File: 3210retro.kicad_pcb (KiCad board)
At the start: 4 copper layers, 44 x 118 mm, 200 parts, among them J1101 MICRO_SD_HINGE, J801 TEST_2P, P101 USB_OTG, P107 HEADPHONE, P109 RUMBLE, P301 SEPS525, P801 JTAG, Q501 MMBF170, Q701 MMBF170, SW701 SW_PUSH, SW702 C, SW703 1, SW704 4ghi, SW705 7pqrs, SW706 -, SW707 2abc, SW708 5jkl, SW709 8tuv, SW710 UP, SW711 3def, SW712 6mno, SW713 9wxyz, SW714 *+, SW715 DOWN, SW716 0space, SW717 #up, U1102 EMIF06-mSD02C3, U1301 LSM9DS1, U201 MAX1555, U202 TPS62742, U203 TPS61021A, U301 TPS61041DBV, U401 LD3985G18R_TSOT23, U402 DRV8601, U403 WM8994ECS/R, U404 MP34DT01TR, U405 MP34DT01TR, U501 SN74AVC2T244, U502 SN74AVC2T244, U503 SN74AVC2T244, U504 A7, U505 SIM_SLOT, U506 SN74AVC2T244, U601 ESP-12E, U801 STM32F756VGTx, X101 ANT_GPS, X102 ANT_GSM, Y801 32kHz, Y802 24MHz

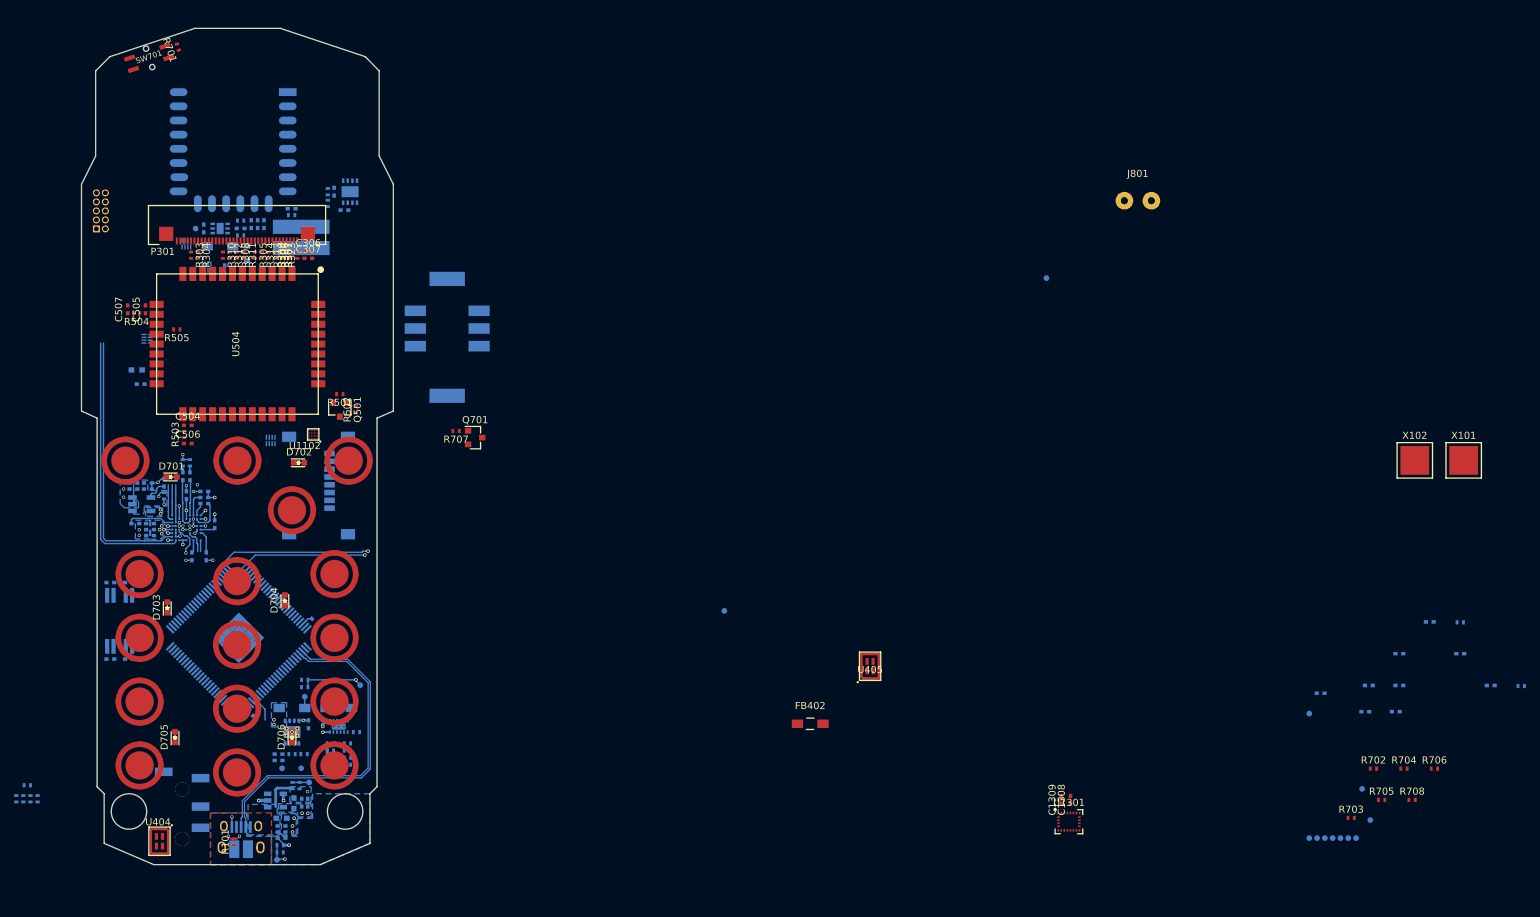
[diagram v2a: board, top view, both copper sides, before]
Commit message: Revision 1 of Layout
6layer board
through-hole via only (0.5/0.3mm drill)
0.2mm track width

https://hackaday.io/project/21263-nokia-3210-retro-fit-board/log/66914-prototype-pcb-done-there-comes-the-review
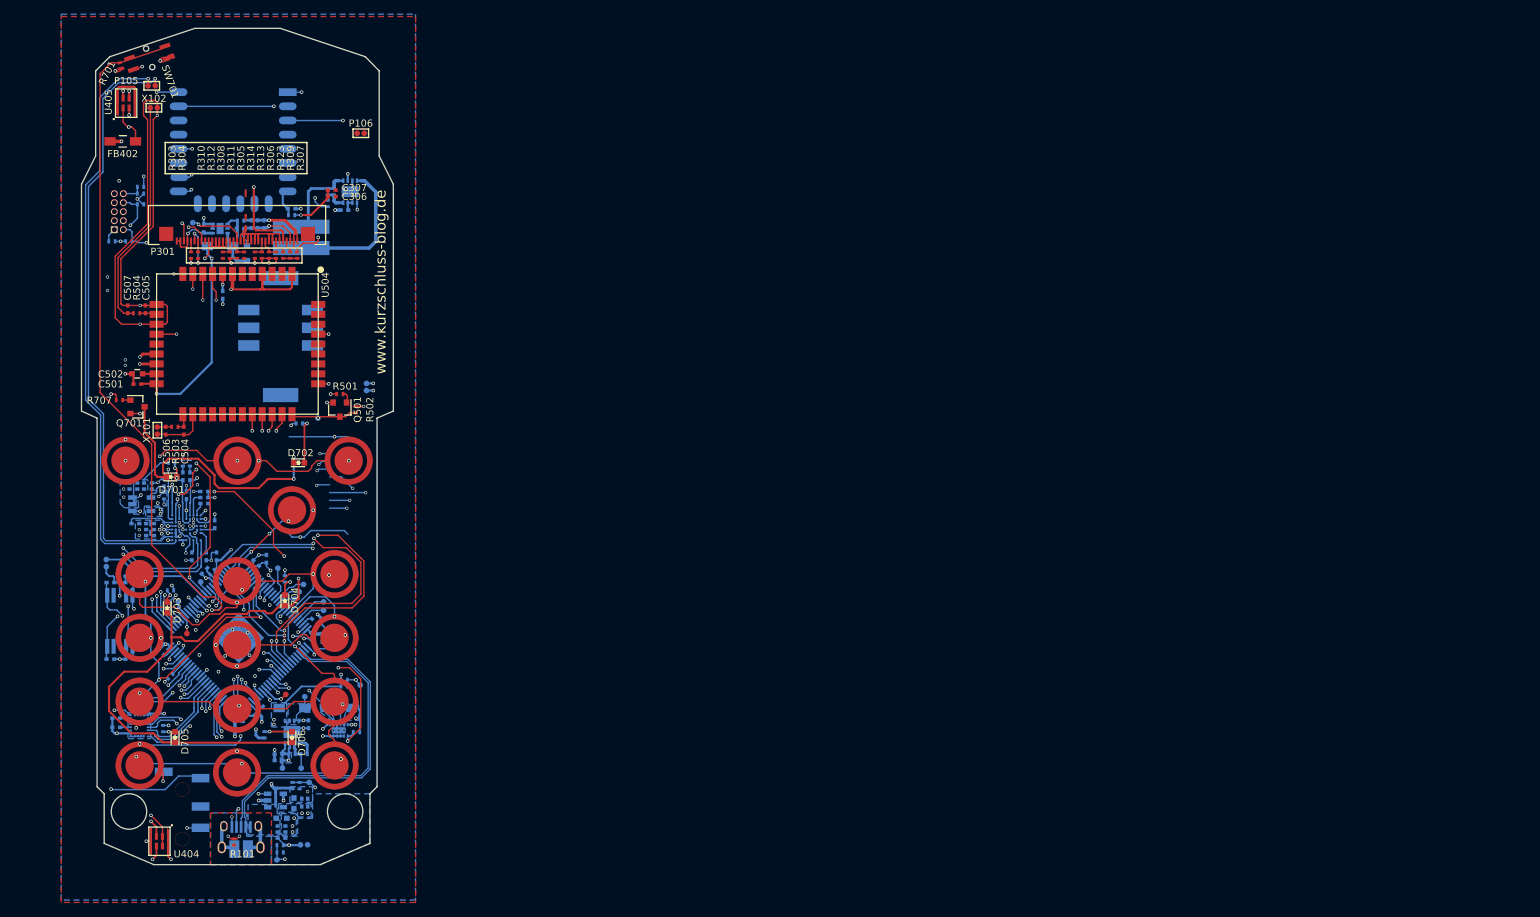
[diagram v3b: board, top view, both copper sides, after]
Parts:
- removed J1101: MICRO_SD_HINGE, Connectors:microSD_Card_Receptacle_Wuerth_693072010801
- removed R205, R206, R209, R210, R211, R212, R213, R214: 0, Resistors_SMD:R_0402_NoSilk
- removed R505: 100, Resistors_SMD:R_0402_NoSilk
- removed TP701, TP702, TP703, TP704, TP705, TP706, TP707, TP708, TP709, TP801: TP, NokiaRetroFit:TP
- removed U1102: EMIF06-mSD02C3, NokiaRetroFit:EMIF06-mSD02C3
- removed U501, U502, U503, U506: SN74AVC2T244, NokiaRetroFit:SN74AVC2T244
- added P103: LIPO, NokiaRetroFit:SolderWirePad_2x_0,8, B.Cu at (117.6, 91.7)
- added P104: DC, NokiaRetroFit:SolderWirePad_2x_0,8, B.Cu at (108.8, 156.3)
- added P105: EAR, NokiaRetroFit:SolderWirePad_2x_0,8, F.Cu at (87.3, 49.2)
- added P106: SPEAKER, NokiaRetroFit:SolderWirePad_2x_0,8, F.Cu at (116.8, 55.9)
- added TP102: TP, NokiaRetroFit:TP, B.Cu at (92.3, 126.5)
- added TP103: TP, NokiaRetroFit:TP, F.Cu at (105.1, 117.3)
- added TP104: TP, NokiaRetroFit:TP, F.Cu at (108.7, 119.6)
- added TP105: TP, NokiaRetroFit:TP, F.Cu at (108.1, 120.6)
- added TP106: TP, NokiaRetroFit:TP, F.Cu at (107.5, 121.6)
- added TP107: TP, NokiaRetroFit:TP, F.Cu at (94.2, 119.2)
- added TP108: TP, NokiaRetroFit:TP, F.Cu at (91.0, 122.0)
- added TP109: TP, NokiaRetroFit:TP, F.Cu at (111.5, 122.0)
- added TP110: TP, NokiaRetroFit:TP, F.Cu at (111.5, 123.2)
- C1308, C1309, R702, R703, R704, R705, R706, R708, TP101, U1301: moved to B.Cu
- C501, C502: moved to F.Cu
- J801: footprint Wire_Pads:SolderWirePad_2x_1mmDrill -> NokiaRetroFit:SolderWirePad_2x_0,8; moved to B.Cu
- U203: footprint Housings_SON:Texas_S-PVSON-N8_ThermalVias -> NokiaRetroFit:Texas_S-PVSON-N8_NoThermalVias
- U404, U405: footprint NokiaRetroFit:MP34DT01 -> NokiaRetroFit:MP34DT01_NoGroundRing
- X101, X102: footprint SMD_Packages:1Pin -> NokiaRetroFit:SolderWirePad_2x_0,8
- moved R803 185.4 mm to (95.8, 117.8), turned to 45 degrees
- moved X102 184.8 mm to (87.6, 52.3)
- moved X101 184.4 mm to (88.1, 97.8), turned to 270 degrees
- moved R802 182.2 mm to (89.9, 132.5), turned to 225 degrees
- moved C805 179.5 mm to (84.1, 118.4), turned to 180 degrees
- moved R706 179.5 mm to (88.9, 139.9), turned to 270 degrees
- moved C814 176.7 mm to (99.6, 138.9)
- moved R704 175.8 mm to (90.0, 120.4), turned to 180 degrees
- moved R702 175.0 mm to (90.1, 102.4)
- moved C815 172.6 mm to (99.6, 138.0)
- moved C809 170.1 mm to (88.6, 129.1), turned to 315 degrees
- moved C808 169.4 mm to (94.7, 117.6), turned to 225 degrees
- moved C813 167.8 mm to (96.4, 115.6), turned to 90 degrees
- moved R708 162.2 mm to (103.2, 140.8), turned to 90 degrees
- moved R703 158.5 mm to (108.1, 96.8)
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- renumbered P109 to P108
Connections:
- C809 pad 1: NVCC_3V3 -> 3V3
- C810 pad 1: NVCC_3V3 -> 3V3
- C811 pad 1: NVCC_3V3 -> 3V3
- C812 pad 1: NVCC_3V3 -> 3V3
- C813 pad 1: NVCC_3V3 -> 3V3
- C814 pad 1: NVCC_3V3 -> 3V3
- C815 pad 1: NVCC_3V3 -> 3V3
- FB402 pad 1: +3V3 -> NVCC_3V3
- P108 pad 1: (no net) -> /Audio Amplifier/RMBL-
- P801 pad 7: Net-(P801-Pad7) -> (no net)
- R701 pad 1: VSNVS -> 3V3
- R801 pad 1: VLDO3_3V3 -> NVCC_3V3
- R803 pad 2: NVCC_3V3 -> 3V3
- R804 pad 1: VLDO3_3V3 -> NVCC_3V3
- R805 pad 1: VLDO3_3V3 -> NVCC_3V3
- R807 pad 1: VLDO3_3V3 -> NVCC_3V3
- U202 pad 10: Net-(R206-Pad1) -> +BATT_LIPO
- U202 pad 11: Net-(R205-Pad1) -> +BATT_LIPO
- U202 pad 8: Net-(R210-Pad1) -> +BATT_LIPO
- U202 pad 9: Net-(R209-Pad1) -> +BATT_LIPO
- U403 pad A2: /Audio Amplifier/SPK_- -> /Audio Amplifier/SPK_OUT-
- U403 pad B1: /Audio Amplifier/SPK_+ -> /Audio Amplifier/SPK_OUT+
- U403 pad D6: GND -> GNDA
- U403 pad E7: GND -> GNDA
- U403 pad E8: GND -> GNDA
- U504 pad 10: Net-(U501-Pad7) -> /Radio Module, GPS and SIM/AT_UART_RTS
- U504 pad 11: Net-(U501-Pad6) -> /Radio Module, GPS and SIM/AT_UART_CTS
- U504 pad 26: /Audio Amplifier/SPK_+ -> /Radio Module, GPS and SIM/SPK_+
- U504 pad 27: /Audio Amplifier/SPK_- -> /Radio Module, GPS and SIM/SPK_-
- U504 pad 30: Net-(U502-Pad7) -> /Radio Module, GPS and SIM/AT_UART_TX
- U504 pad 31: Net-(U502-Pad6) -> /Radio Module, GPS and SIM/AT_UART_RX
- U504 pad 32: Net-(U503-Pad7) -> /Radio Module, GPS and SIM/HST_RX
- U504 pad 33: Net-(U503-Pad6) -> /Radio Module, GPS and SIM/HST_TX
- U504 pad 37: Net-(R505-Pad2) -> /Radio Module, GPS and SIM/GPS_TX
- U801 pad 100: NVCC_3V3 -> 3V3
- U801 pad 101: (no net) -> GND
- U801 pad 11: NVCC_3V3 -> 3V3
- U801 pad 21: NVCC_3V3 -> 3V3
- U801 pad 27: NVCC_3V3 -> 3V3
- U801 pad 50: NVCC_3V3 -> 3V3
- U801 pad 75: NVCC_3V3 -> 3V3
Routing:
- net NVCC_3V3: track 1.82 -> 235.5 mm, vias 2 -> 21
- net 4V_BST: track 1.64 -> 196.5 mm, vias 1 -> 7
- net 3V3: track 0.00 -> 188.2 mm, vias 0 -> 8
- net GND: track 22.2 -> 204.6 mm, vias 26 -> 76
- net /Buttons and LEDs/KEYPAD_ROW3: track 0.00 -> 150.9 mm, vias 0 -> 6
- net Net-(U403-PadC6): track 3.29 -> 139.5 mm, vias 0 -> 3
- net Net-(U403-PadA9): track 1.60 -> 130.6 mm, vias 0 -> 3
- net Net-(D701-Pad1): track 0.00 -> 125.1 mm, vias 0 -> 3
- net GNDA: track 0.00 -> 116.0 mm, vias 0 -> 3
- net Net-(FB402-Pad2): track 0.00 -> 115.5 mm, vias 0 -> 2
- net /Audio Amplifier/RMBL_PWM: track 0.00 -> 108.3 mm, vias 0 -> 3
- net /Controller/WIFI_CHPD: track 0.00 -> 105.3 mm, vias 0 -> 2
- net /Controller/WIFI_RESET: track 0.00 -> 103.7 mm, vias 0 -> 2
- net /Controller/JTAG_TDO: track 0.00 -> 103.0 mm, vias 0 -> 1
- net /Controller/JTAG_RST: track 0.00 -> 102.9 mm, vias 0 -> 2
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- added copper zone on POWER, net /Radio Module, GPS and SIM/GSM_GND
- added copper zone on B.Cu, net 3V3
- added copper zone on F.Cu, net 3V3
- added copper zone on POWER, net 3V3
- added copper zone on B.Cu, net 4V_BST
- added copper zone on F.Cu, net GND
- added copper zone on GND, net GND
- added copper zone on POWER, net NVCC_3V3
- added copper zone on B.Cu, net Net-(L201-Pad2)
- added copper zone on B.Cu, net Net-(L202-Pad1)
- removed copper zone on TOP_GND, net GND
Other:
- copper layers 4 -> 6
- board text added: "Nokia 3210 Retro Fit Board V1.0"
- board text added: "www.kurzschluss-blog.de"

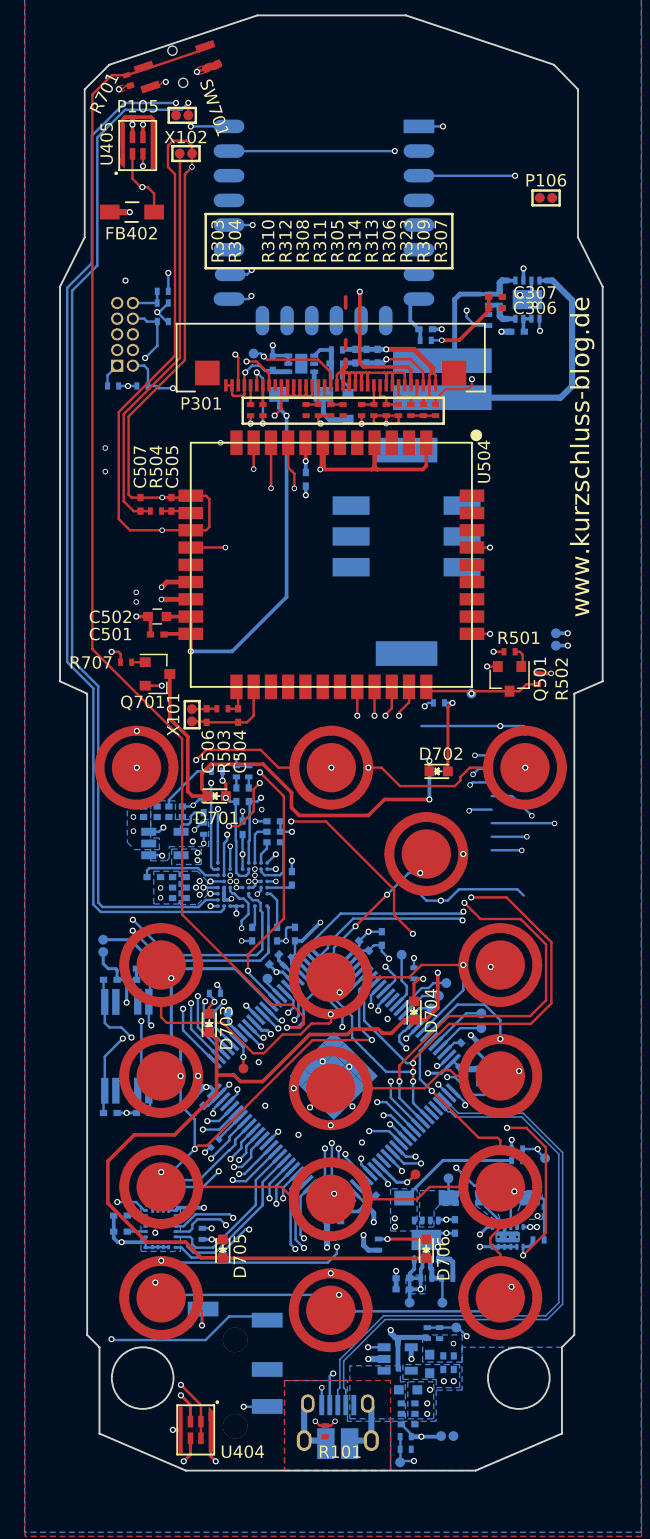
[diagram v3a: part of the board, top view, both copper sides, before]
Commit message: Board modified to actual measurements
* rumble motor was on the wrong side of the board. fixed
* some drill holes where missing
* moved voice mic to bottom side. top side is completely
  enclosed by the case
* several small fixes
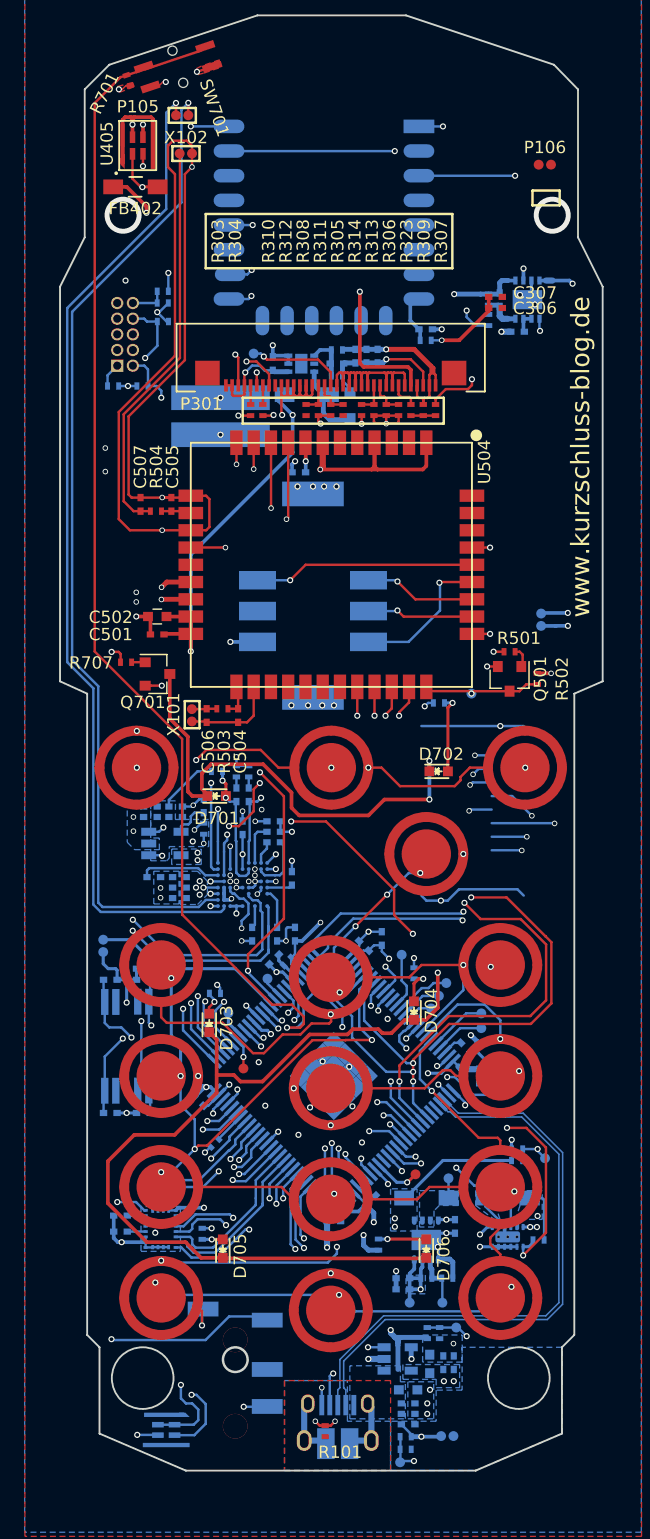
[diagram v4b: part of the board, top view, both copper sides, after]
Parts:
- U404: moved to B.Cu
- moved P108 18.2 mm to (90.4, 75.1)
- moved U505 8.38 mm to (97.9, 88.2), turned to 180 degrees
- moved P106 2.70 mm to (116.7, 53.2)
- moved U404 2.39 mm to (86.0, 155.8), turned to 270 degrees
- moved FB402 2.07 mm to (83.5, 55.0)
- moved P103 2.00 mm to (116.4, 90.1)
- moved C503 0.80 mm to (96.8, 78.2), turned to 180 degrees
- moved L303 0.46 mm to (97.4, 71.8)
- moved D301 0.20 mm to (100.9, 72.7)
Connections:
- P801 pad 7: (no net) -> Net-(P801-Pad7)
- U301 pad 1: GND -> (no net)
- U301 pad 2: 4V_BST -> (no net)
- U301 pad 3: 4V_BST -> (no net)
- U301 pad 4: Net-(C304-Pad2) -> (no net)
- U301 pad 6: Net-(D301-Pad2) -> (no net)
- U402 pad 1: /Audio Amplifier/RMBL_EN -> (no net)
- U402 pad 2: Net-(C402-Pad1) -> (no net)
- U402 pad 3: Net-(C402-Pad1) -> (no net)
- U402 pad 4: Net-(C407-Pad2) -> (no net)
- U402 pad 5: /Audio Amplifier/RMBL+ -> (no net)
- U402 pad 6: 4V_BST -> (no net)
- U402 pad 7: GND -> (no net)
- U402 pad 8: /Audio Amplifier/RMBL- -> (no net)
- U402 pad 9: GND -> (no net)
- U505 pad 2: GND -> Net-(U504-Pad14)
- U505 pad 3: Net-(U504-Pad14) -> Net-(U504-Pad15)
- U505 pad 4: Net-(U504-Pad16) -> GND
- U505 pad 5: Net-(U504-Pad15) -> (no net)
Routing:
- net /Audio Amplifier/RMBL+: track 11.6 -> 31.4 mm, vias 0 -> 2
- net Net-(U504-Pad17): track 0.00 -> 17.9 mm, vias 0 -> 1
- net /Audio Amplifier/RMBL-: track 21.2 -> 36.4 mm, vias 0 -> 2
- net Net-(U504-Pad16): track 0.00 -> 11.8 mm, vias 0 -> 1
- net Net-(U504-Pad15): track 0.00 -> 9.03 mm, vias 0 -> 1
- net Net-(U504-Pad14): track 0.00 -> 8.62 mm, vias 0 -> 1
- net /Controller/WIFI_BOOT0: track 87.5 -> 82.5 mm
- net GND: track 204.6 -> 200.2 mm, vias 76 -> 81
- net Net-(U403-PadA9): track 130.6 -> 134.4 mm
- net (no net): track 0.00 -> 2.83 mm, vias 1 -> 3
- net +BATT_LIPO: track 80.5 -> 83.3 mm
- net /Audio Amplifier/SPK_OUT+: track 83.4 -> 80.7 mm
- net /Audio Amplifier/SPK_OUT-: track 84.1 -> 81.7 mm
- net /Radio Module, GPS and SIM/HST_TX: track 86.7 -> 88.9 mm
- net NVCC_3V3: track 235.5 -> 237.7 mm, vias 21 -> 23
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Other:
- outline, holes or cut-outs redrawn
